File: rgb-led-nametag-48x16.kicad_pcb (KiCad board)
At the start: 4 copper layers, 84 x 28.8 mm, 177 parts, among them J1 USB_C_Receptacle_USB2.0, Q1 CJ3139K, Q10 CJ3139K, Q11 CJ3139K, Q12 CJ3139K, Q13 CJ3139K, Q14 CJ3139K, Q15 CJ3139K, Q16 CJ3139K, Q17 CJ3139K, Q18 CJ3139K, Q19 2SK3541, Q2 CJ3139K, Q20 AO3401A, Q21 FS8205A, Q3 CJ3139K, Q4 CJ3139K, Q5 CJ3139K, Q6 CJ3139K, Q7 CJ3139K, Q8 CJ3139K, Q9 CJ3139K, SW1 SW_Push, SW2 SW_Push, U1 led-panel-16x16, U10 74HC595, U11 74HC595, U12 74HC595, U13 74HC595, U14 74HC595, U15 74HC595, U16 led-panel-16x16, U17 74HC595, U18 74HC595, U19 74HC595, U2 74HC595, U20 74HC595, U21 74HC595, U22 74HC595, U23 74HC595, U24 ESP32-PICO-D4, U25 STM32F722RETx, U26 SRV05-4, U27 TPS63001, U28 XC6206P332MR, U29 BQ24081, U3 74HC595, U30 DW01+G, U4 74HC595, U5 74HC595, U6 74HC595, U7 74HC595, U8 74HC595, U9 led-panel-16x16

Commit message: Improve layout
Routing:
- net VBUS: track 419.8 -> 429.5 mm, vias 83 -> 84
- net /~CHRG: track 27.4 -> 24.9 mm
- net /EN: track 66.9 -> 65.4 mm
- net /QSPI_CLK: track 176.1 -> 174.8 mm
- net /Panel 3/R6: track 6.22 -> 5.03 mm
- net /SWDIO: track 25.9 -> 24.7 mm
- net /sheet61C56D2D/SIN: track 30.7 -> 29.6 mm
- net /SPI2_CLK: track 87.4 -> 88.4 mm
- net /Panel 1/R14: track 14.9 -> 13.9 mm
- net /~ESP_EN: track 57.9 -> 56.9 mm
- net /Panel 2/G11: track 5.89 -> 6.80 mm
- net /COL_~OE: track 200.7 -> 199.8 mm
- net /PWR_EN: track 48.3 -> 47.5 mm
- net /Panel 1/G14: track 12.5 -> 11.8 mm
- net /A16: track 67.4 -> 66.7 mm
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
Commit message: More layout improvements
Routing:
- net /PWR_EN: track 47.5 -> 46.9 mm
- net /DFU: track 81.9 -> 81.3 mm
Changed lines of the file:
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@@
     (thickness 1.6)
     (drawings 45)
-    (tracks 4904)
+    (tracks 4900)
     (zones 0)
     (modules 177)
@@
   (segment (start 143.83 112.845) (end 140.02 112.845) (width 0.127) (layer In2.Cu) (net 374))
   (segment (start 139.7 113.165) (end 138.165 113.165) (width 0.127) (layer In2.Cu) (net 374))
-  (segment (start 135.375 111.6) (end 133.2 109.425) (width 0.127) (layer In2.Cu) (net 374))
-  (segment (start 133.2 109.425) (end 132.6 109.425) (width 0.127) (layer In2.Cu) (net 374))
   (via (at 110.325 113.325) (size 0.45) (drill 0.2) (layers F.Cu B.Cu) (net 374))
   (segment (start 110.325 113.325) (end 110.325 114.8) (width 0.127) (layer F.Cu) (net 374))
@@
   (segment (start 136.1 112.325) (end 136.55 112.775) (width 0.127) (layer In2.Cu) (net 374))
   (segment (start 138.165 113.165) (end 137.775 112.775) (width 0.127) (layer In2.Cu) (net 374))
-  (segment (start 132.25 109.775) (end 132 110.025) (width 0.127) (layer In2.Cu) (net 374))
-  (segment (start 132.6 109.425) (end 132.25 109.775) (width 0.127) (layer In2.Cu) (net 374))
   (segment (start 110.325 111.55) (end 110.325 113.325) (width 0.127) (layer In2.Cu) (net 374))
   (segment (start 111.775 110.1) (end 110.325 111.55) (width 0.127) (layer In2.Cu) (net 374))
@@
   (segment (start 127.375 110.025) (end 125.475 111.925) (width 0.127) (layer In2.Cu) (net 374))
   (segment (start 127.925 110.025) (end 127.375 110.025) (width 0.127) (layer In2.Cu) (net 374))
-  (segment (start 132 110.025) (end 127.925 110.025) (width 0.127) (layer In2.Cu) (net 374))
   (segment (start 121.7375 109.8125) (end 118.7125 109.8125) (width 0.127) (layer In2.Cu) (net 374))
   (segment (start 127.925 110.025) (end 127.775 110.025) (width 0.127) (layer In2.Cu) (net 374))
+  (segment (start 133.8 110.025) (end 134.55 110.775) (width 0.127) (layer In2.Cu) (net 374))
+  (segment (start 131.625 110.025) (end 133.8 110.025) (width 0.127) (layer In2.Cu) (net 374))
+  (segment (start 135.375 111.6) (end 134.55 110.775) (width 0.127) (layer In2.Cu) (net 374))
+  (segment (start 131.625 110.025) (end 127.925 110.025) (width 0.127) (layer In2.Cu) (net 374))
   (segment (start 110.143287 105.517625) (end 111.317956 104.342956) (width 0.127) (layer F.Cu) (net 375))
   (segment (start 114.032375 109.406713) (end 114.032375 109.417625) (width 0.127) (layer F.Cu) (net 376))
@@
   (segment (start 147.47 111.505) (end 147.325 111.65) (width 0.127) (layer F.Cu) (net 380))
   (segment (start 147.47 110.655) (end 147.47 111.505) (width 0.127) (layer F.Cu) (net 380))
-  (segment (start 133.3 109.075) (end 132.5 109.075) (width 0.127) (layer In2.Cu) (net 380))
   (via (at 109.835 112.685) (size 0.45) (drill 0.2) (layers F.Cu B.Cu) (net 380))
   (segment (start 109.34 112.685) (end 109.835 112.685) (width 0.127) (layer B.Cu) (net 380))
@@
   (segment (start 139.54 111.895) (end 139.0475 111.4025) (width 0.127) (layer In2.Cu) (net 380))
   (segment (start 135.4375 111.2125) (end 135.925 111.7) (width 0.127) (layer In2.Cu) (net 380))
-  (segment (start 135.4375 111.2125) (end 133.3 109.075) (width 0.127) (layer In2.Cu) (net 380))
   (segment (start 137.85 111.7) (end 137.875 111.675) (width 0.127) (layer In2.Cu) (net 380))
   (segment (start 135.925 111.7) (end 137.85 111.7) (width 0.127) (layer In2.Cu) (net 380))
   (segment (start 138.1475 111.4025) (end 137.875 111.675) (width 0.127) (layer In2.Cu) (net 380))
-  (segment (start 132.5 109.075) (end 132.175 109.4) (width 0.127) (layer In2.Cu) (net 380))
   (segment (start 109.835 111.59) (end 109.835 112.685) (width 0.127) (layer In2.Cu) (net 380))
   (segment (start 111.625 109.8) (end 109.835 111.59) (width 0.127) (layer In2.Cu) (net 380))
@@
   (segment (start 127.25 109.75) (end 125.375 111.625) (width 0.127) (layer In2.Cu) (net 380))
   (segment (start 131.825 109.75) (end 127.25 109.75) (width 0.127) (layer In2.Cu) (net 380))
-  (segment (start 132.175 109.4) (end 131.825 109.75) (width 0.127) (layer In2.Cu) (net 380))
+  (segment (start 133.975 109.75) (end 134.125 109.9) (width 0.127) (layer In2.Cu) (net 380))
+  (segment (start 131.825 109.75) (end 133.975 109.75) (width 0.127) (layer In2.Cu) (net 380))
+  (segment (start 135.4375 111.2125) (end 134.125 109.9) (width 0.127) (layer In2.Cu) (net 380))
   (via (at 118.5 111.375) (size 0.45) (drill 0.2) (layers F.Cu B.Cu) (net 381))
   (segment (start 118.5 111.375) (end 118.5 110.775) (width 0.127) (layer F.Cu) (net 381))
@@
   (segment (start 136.68 111.055) (end 136.825 111.2) (width 0.127) (layer B.Cu) (net 427))
   (segment (start 136.68 110.805) (end 136.68 111.055) (width 0.127) (layer B.Cu) (net 427))
-  (segment (start 135.85 111.2) (end 133.425 108.775) (width 0.127) (layer In2.Cu) (net 427))
-  (segment (start 133.425 108.775) (end 132.375 108.775) (width 0.127) (layer In2.Cu) (net 427))
   (segment (start 136.825 111.2) (end 135.85 111.2) (width 0.127) (layer In2.Cu) (net 427))
   (segment (start 137.96 107.175) (end 136.68 108.455) (width 0.127) (layer B.Cu) (net 427))
   (segment (start 139 107.175) (end 137.96 107.175) (width 0.127) (layer B.Cu) (net 427))
   (segment (start 136.68 108.455) (end 136.68 110.805) (width 0.127) (layer B.Cu) (net 427))
-  (segment (start 132.375 108.775) (end 132.15 109) (width 0.127) (layer In2.Cu) (net 427))
   (segment (start 123.55 109.7) (end 123.55 109.475) (width 0.127) (layer In2.Cu) (net 427))
   (segment (start 123.375 109.875) (end 123.55 109.7) (width 0.127) (layer In2.Cu) (net 427))
@@
   (segment (start 131.675 109.475) (end 127.1 109.475) (width 0.127) (layer In2.Cu) (net 427))
   (segment (start 127.1 109.475) (end 125.25 111.325) (width 0.127) (layer In2.Cu) (net 427))
-  (segment (start 132.15 109) (end 131.675 109.475) (width 0.127) (layer In2.Cu) (net 427))
+  (segment (start 134.125 109.475) (end 134.25 109.6) (width 0.127) (layer In2.Cu) (net 427))
+  (segment (start 131.675 109.475) (end 134.125 109.475) (width 0.127) (layer In2.Cu) (net 427))
+  (segment (start 135.85 111.2) (end 134.25 109.6) (width 0.127) (layer In2.Cu) (net 427))
   (segment (start 139.775 111.225) (end 139.775 110.425) (width 0.127) (layer F.Cu) (net 428))
   (segment (start 139.775 110.425) (end 138.975 109.625) (width 0.127) (layer F.Cu) (net 428))
@@
   (segment (start 123.1 107.975) (end 123.41 107.975) (width 0.127) (layer In2.Cu) (net 436))
   (segment (start 117.48 107.975) (end 123.1 107.975) (width 0.127) (layer In2.Cu) (net 436))
-  (segment (start 132.00401 108.22099) (end 131.20401 108.22099) (width 0.127) (layer In2.Cu) (net 436))
-  (segment (start 132.005 108.22) (end 132.00401 108.22099) (width 0.127) (layer In2.Cu) (net 436))
-  (segment (start 132.005 108.205) (end 132.005 108.22) (width 0.127) (layer In2.Cu) (net 436))
-  (segment (start 133.63 108.205) (end 132.005 108.205) (width 0.127) (layer In2.Cu) (net 436))
   (segment (start 131.20401 108.22099) (end 130.5 108.925) (width 0.127) (layer In2.Cu) (net 436))
   (segment (start 130.5 108.925) (end 126.85 108.925) (width 0.127) (layer In2.Cu) (net 436))
@@
   (segment (start 124.405 108.97) (end 123.555 108.12) (width 0.127) (layer In2.Cu) (net 436))
   (segment (start 124.46 109.025) (end 124.405 108.97) (width 0.127) (layer In2.Cu) (net 436))
+  (segment (start 131.22 108.205) (end 131.20401 108.22099) (width 0.127) (layer In2.Cu) (net 436))
+  (segment (start 132.57 108.205) (end 131.22 108.205) (width 0.127) (layer In2.Cu) (net 436))
+  (segment (start 133.63 108.205) (end 132.57 108.205) (width 0.127) (layer In2.Cu) (net 436))
   (segment (start 137.04 114.395) (end 136.03 114.395) (width 0.127) (layer F.Cu) (net 438))
   (segment (start 136.07 112.925) (end 136.97 112.925) (width 0.127) (layer F.Cu) (net 439))

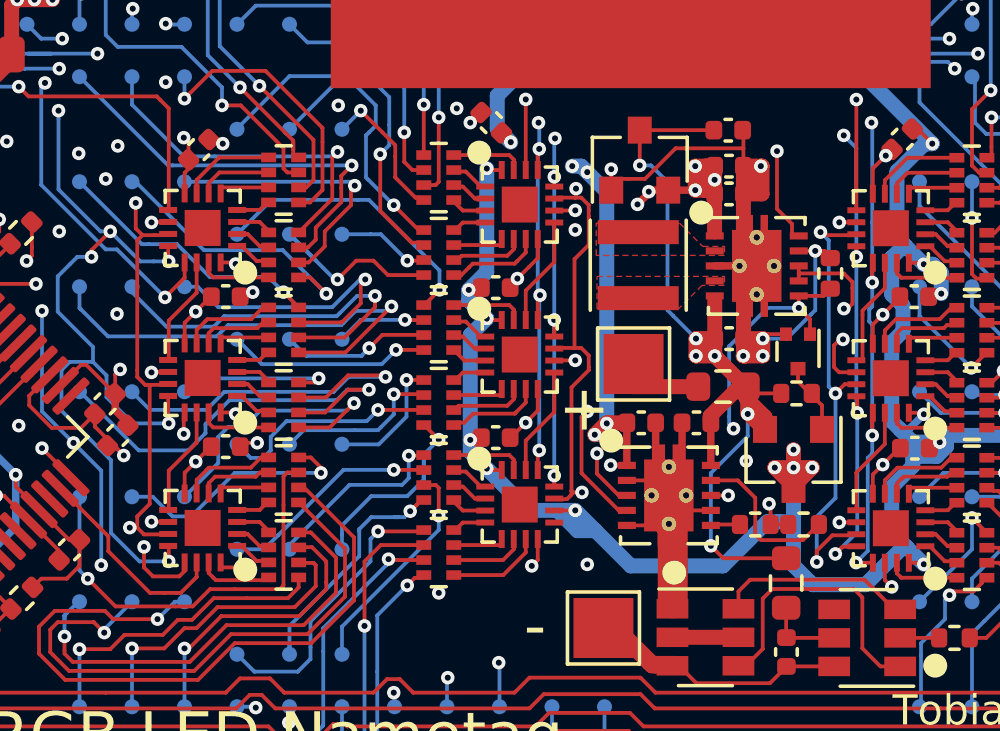
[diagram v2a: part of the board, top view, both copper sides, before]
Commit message: Stitch L1 GND together on L2
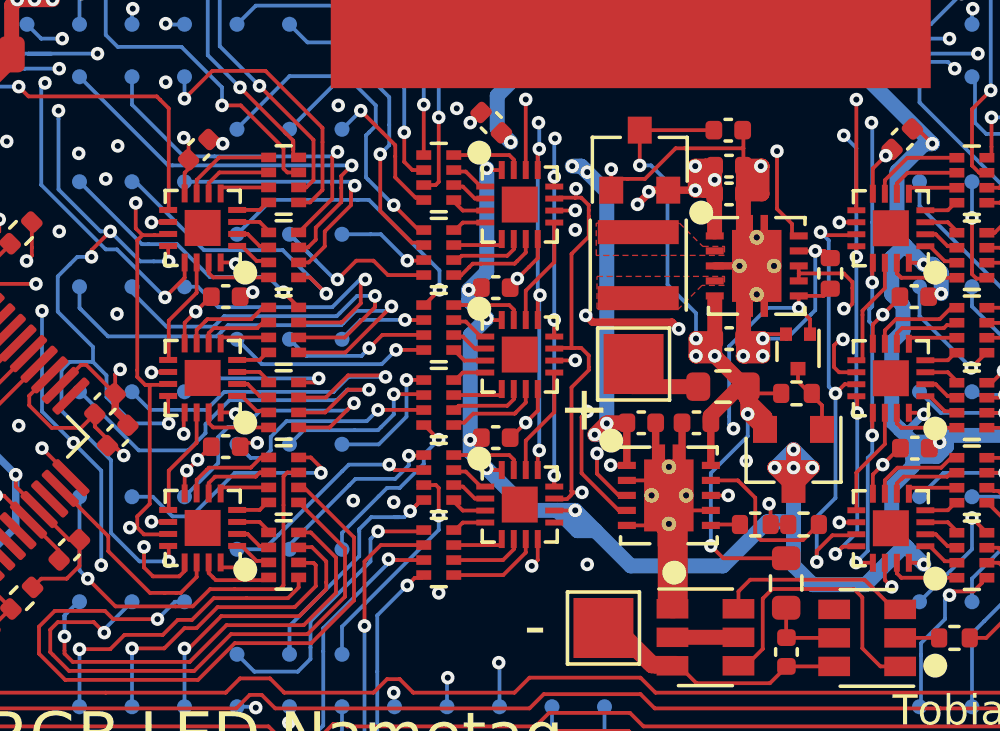
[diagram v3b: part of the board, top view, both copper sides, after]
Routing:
- net GND: track 139.6 -> 152.4 mm, vias 126 -> 131
- net VBUS: track 429.5 -> 437.6 mm
- net /ROW_LATCH: track 87.4 -> 85.1 mm
- net /Panel 2/B5: track 7.05 -> 5.94 mm
- net /EN: track 65.4 -> 66.3 mm

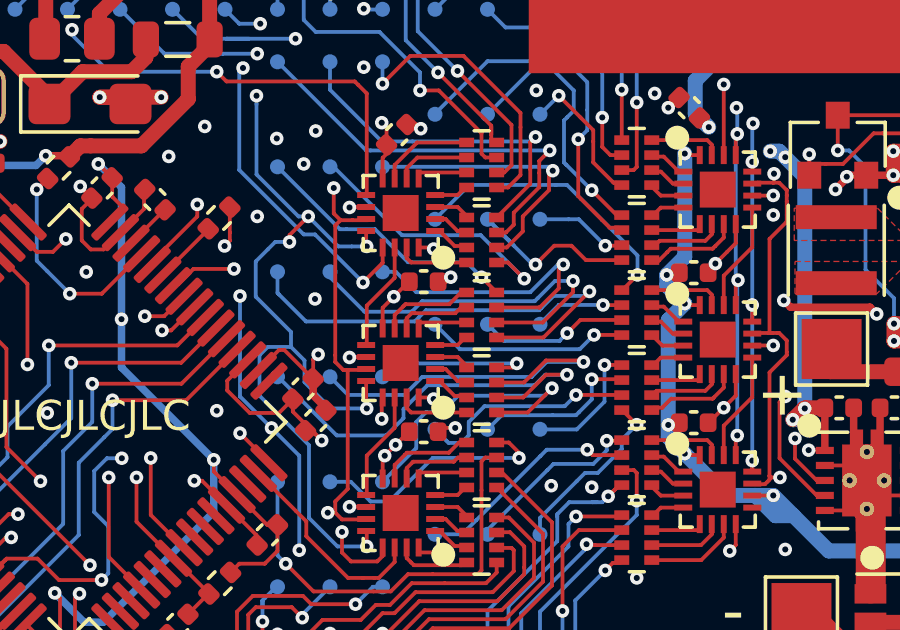
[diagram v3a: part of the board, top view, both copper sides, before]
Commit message: Patch up L1 GND even more
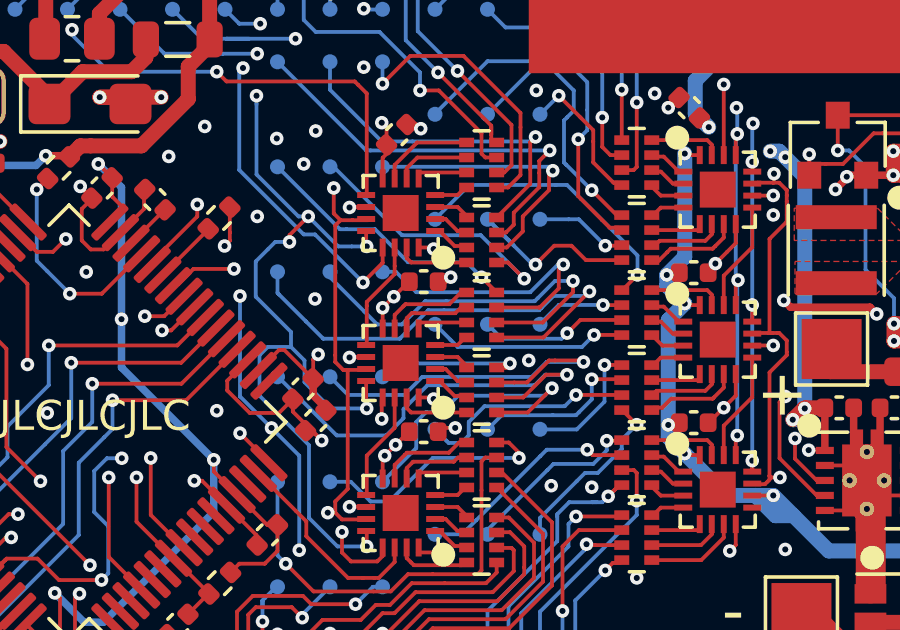
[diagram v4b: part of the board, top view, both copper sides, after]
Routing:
- net GND: track 152.4 -> 159.2 mm, vias 131 -> 133
- net /BOOT: track 55.1 -> 56.3 mm
- net /PWR_EN: track 46.9 -> 45.8 mm
- net /IRQ: track 58.2 -> 57.2 mm

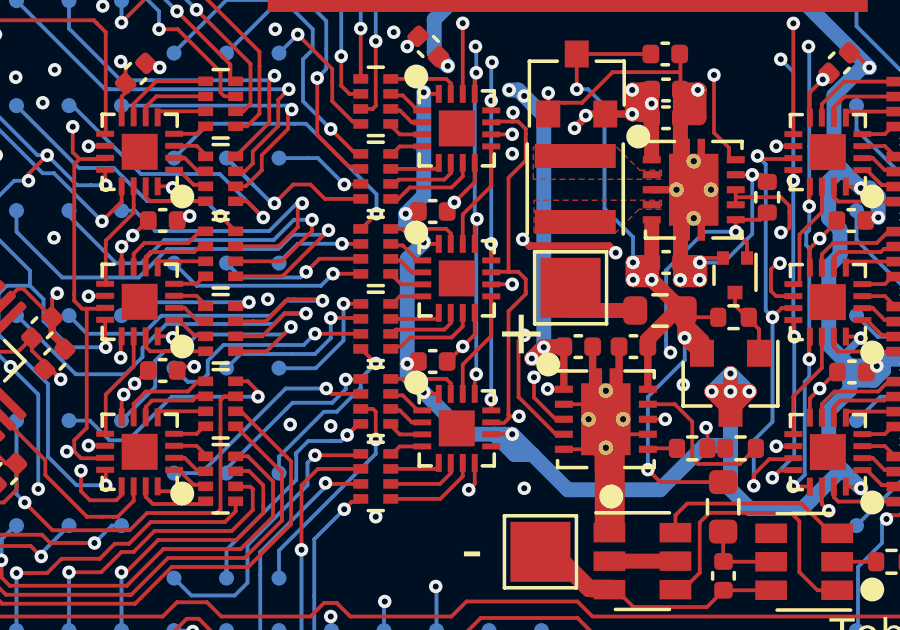
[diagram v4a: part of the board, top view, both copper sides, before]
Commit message: Improve VBUS connectivity
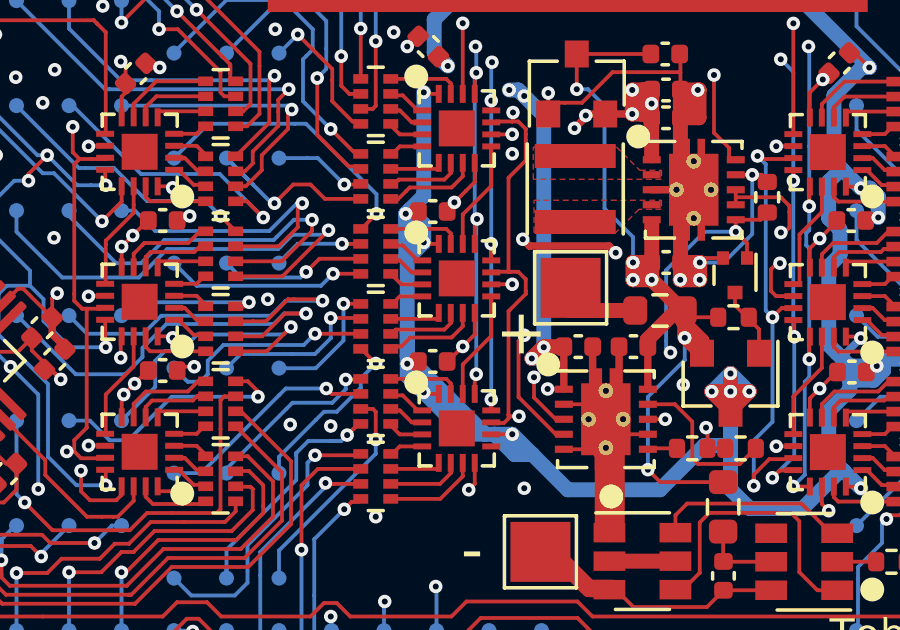
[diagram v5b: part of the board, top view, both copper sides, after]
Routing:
- net VBUS: track 437.6 -> 444.8 mm
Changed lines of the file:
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@@
     (thickness 1.6)
     (drawings 45)
-    (tracks 4966)
+    (tracks 4975)
     (zones 0)
     (modules 177)
@@
   )
   (setup
-    (last_trace_width 0.127)
+    (last_trace_width 0.5)
     (user_trace_width 0.25)
     (user_trace_width 0.5)
@@
   (segment (start 129.4 101.65) (end 129.4 101.73) (width 0.5) (layer In1.Cu) (net 1))
   (segment (start 131.55 108.925) (end 129.995 108.925) (width 0.5) (layer In1.Cu) (net 1))
-  (segment (start 128.6 105.975) (end 128 106.575) (width 0.5) (layer B.Cu) (net 1))
   (segment (start 128.6 102.53) (end 128.6 105.975) (width 0.5) (layer B.Cu) (net 1))
   (segment (start 129.995 108.925) (end 128.6 107.53) (width 0.5) (layer In1.Cu) (net 1))
@@
   (segment (start 128 106.575) (end 128 106.93) (width 0.5) (layer B.Cu) (net 1))
   (segment (start 128.05 108.08) (end 128.6 107.53) (width 0.5) (layer B.Cu) (net 1))
-  (segment (start 128.05 111.575) (end 128.05 108.08) (width 0.5) (layer B.Cu) (net 1))
   (segment (start 128.05 111.98) (end 128.6 112.53) (width 0.5) (layer B.Cu) (net 1))
   (segment (start 128.05 111.575) (end 128.05 111.98) (width 0.5) (layer B.Cu) (net 1))
@@
   (segment (start 132.225 114.6) (end 131.625 114.6) (width 0.5) (layer B.Cu) (net 1))
   (segment (start 131.55 113.925) (end 130.95 113.925) (width 0.5) (layer B.Cu) (net 1))
-  (segment (start 130.95 113.925) (end 129.995 113.925) (width 0.5) (layer B.Cu) (net 1))
   (segment (start 131.55 113.925) (end 132.225 114.6) (width 0.5) (layer B.Cu) (net 1))
   (segment (start 132.225 114.6) (end 133.4 115.775) (width 0.5) (layer B.Cu) (net 1))
@@
   (segment (start 117.98 109.310001) (end 117.439999 109.310001) (width 0.127) (layer F.Cu) (net 1))
   (via (at 117.425 109.325) (size 0.45) (drill 0.2) (layers F.Cu B.Cu) (net 1))
+  (segment (start 128.05 111.325) (end 130.65 113.925) (width 0.5) (layer B.Cu) (net 1))
+  (segment (start 128.05 110.55) (end 128.05 111.325) (width 0.5) (layer B.Cu) (net 1))
+  (segment (start 130.65 113.925) (end 129.995 113.925) (width 0.5) (layer B.Cu) (net 1))
+  (segment (start 130.95 113.925) (end 130.65 113.925) (width 0.5) (layer B.Cu) (net 1))
+  (segment (start 128.05 111.575) (end 128.05 110.55) (width 0.5) (layer B.Cu) (net 1))
+  (segment (start 128.05 110.55) (end 128.05 108.08) (width 0.5) (layer B.Cu) (net 1))
+  (segment (start 128 108.03) (end 128.05 108.08) (width 0.5) (layer B.Cu) (net 1))
+  (segment (start 128 106.575) (end 128 108.03) (width 0.5) (layer B.Cu) (net 1))
+  (segment (start 128.6 106.925) (end 128.125 106.45) (width 0.5) (layer B.Cu) (net 1))
+  (segment (start 128.6 107.53) (end 128.6 106.925) (width 0.5) (layer B.Cu) (net 1))
+  (segment (start 128.125 106.45) (end 128 106.575) (width 0.5) (layer B.Cu) (net 1))
+  (segment (start 128.6 105.975) (end 128.125 106.45) (width 0.5) (layer B.Cu) (net 1))
   (via (at 158.9 108.325) (size 0.45) (drill 0.2) (layers F.Cu B.Cu) (net 2))
   (via (at 169.7 107.4) (size 0.45) (drill 0.2) (layers F.Cu B.Cu) (net 2))

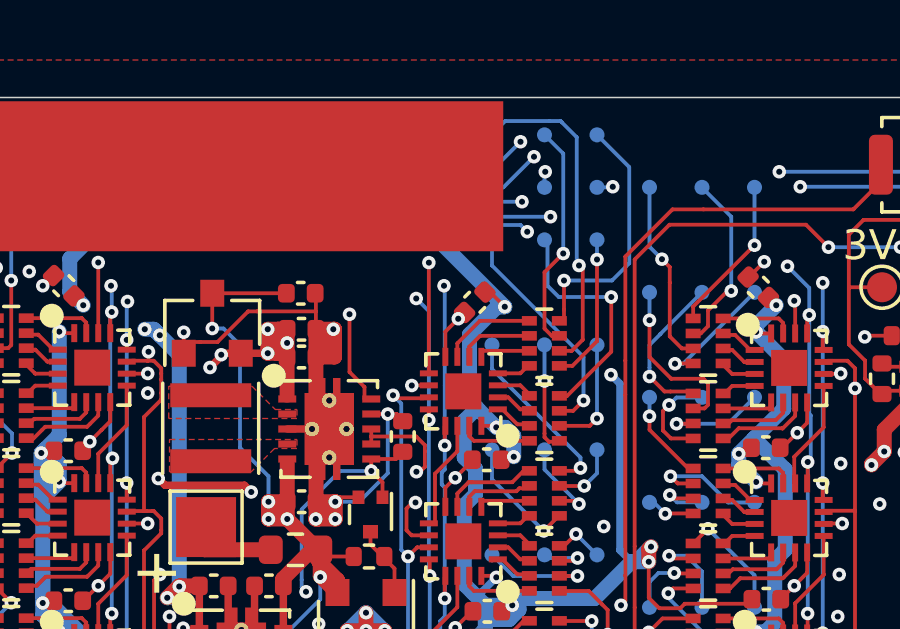
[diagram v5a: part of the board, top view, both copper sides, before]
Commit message: Add more GND via stitching
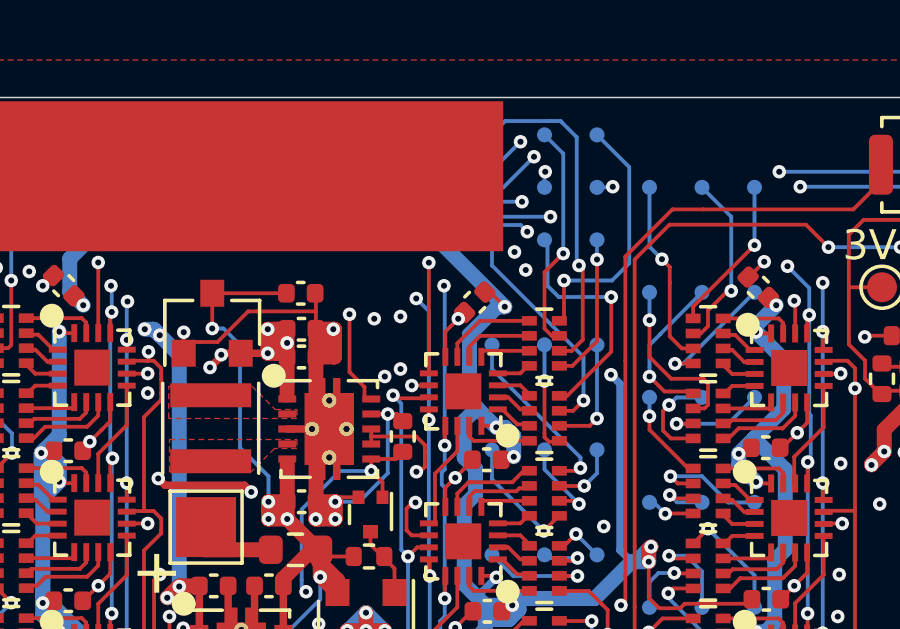
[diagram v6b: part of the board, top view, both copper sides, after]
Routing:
- net GND: vias 133 -> 139
